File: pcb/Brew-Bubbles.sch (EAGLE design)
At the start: 7 parts, among them U1 GP1A57HR, U2 WEMOS-D1-MINI

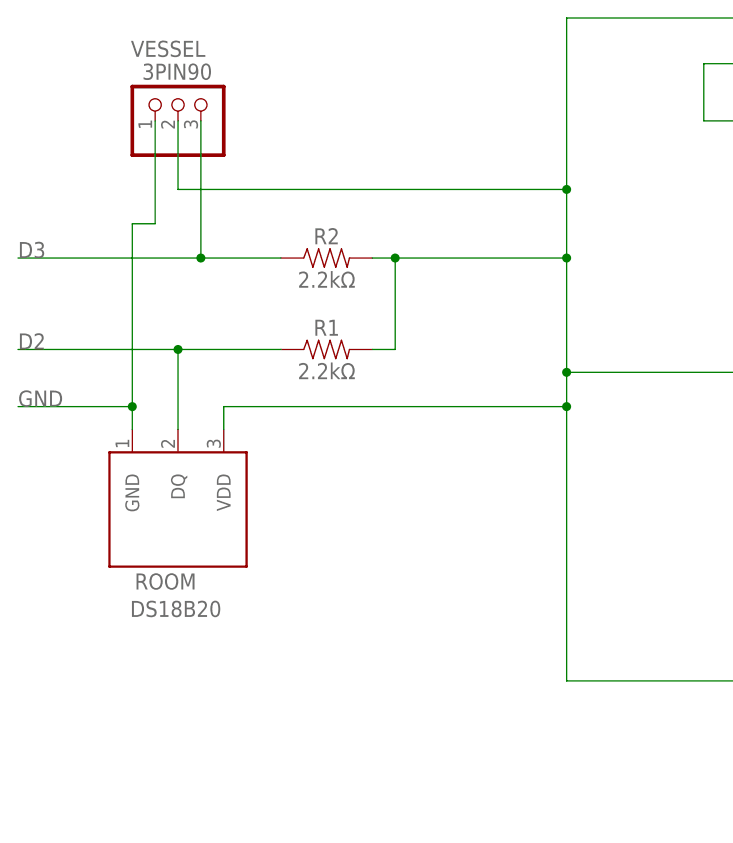
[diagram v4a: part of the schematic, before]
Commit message: Remove onboard sensor move to lead
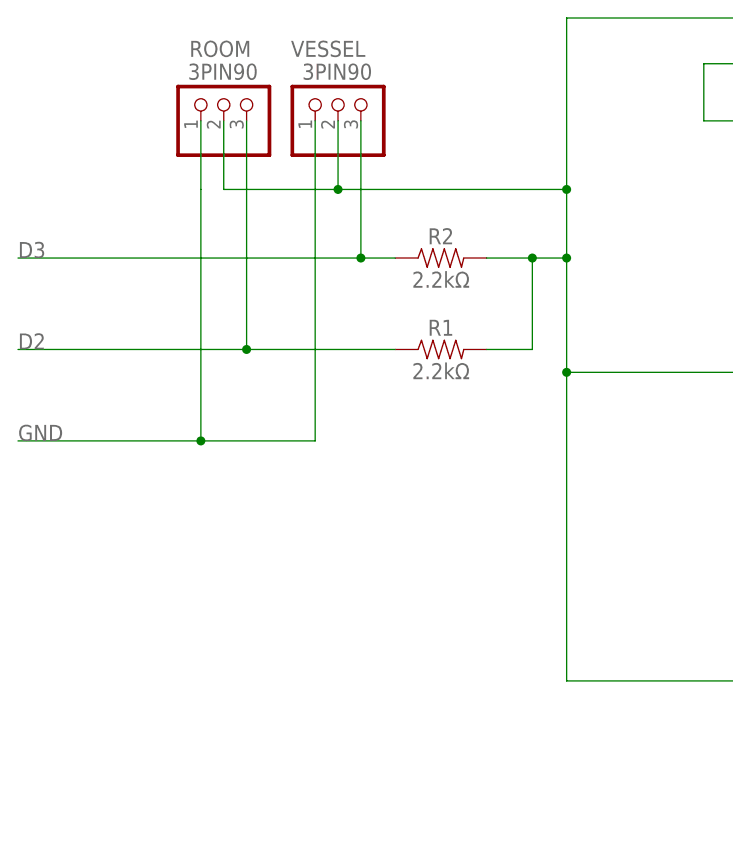
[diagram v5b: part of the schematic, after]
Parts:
- ROOM: value DS18B20 -> 3PIN90; device SparkFun-Sensors:DS18B20 -> pinhead:PINHD-1X3/90
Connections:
- net 3V3: now also ROOM.2; no longer ROOM.VDD
- net D2: now also ROOM.3; no longer ROOM.DQ
- net GND: now also ROOM.1; no longer ROOM.GND
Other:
- moved on the sheet: R1, R2, VESSEL
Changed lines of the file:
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@@
 </classes>
 <parts>
-<part name="ROOM" library="SparkFun-Sensors" deviceset="DS18B20" device=""/>
 <part name="U2" library="diy-modules" deviceset="WEMOS-D1-MINI-SHIELD" device="" value="WEMOS-D1-MINI"/>
 <part name="R1" library="SparkFun-Resistors" deviceset="330OHM" device="-HORIZ-1/10W-5%" value="2.2kΩ"/>
@@
 <part name="U1" library="SparkFun-Sensors" deviceset="GP1A57HR" device=""/>
 <part name="R3" library="SparkFun-Resistors" deviceset="330OHM" device="-HORIZ-1/10W-5%" value="150Ω"/>
+<part name="ROOM" library="pinhead" library_urn="urn:adsk.eagle:library:325" deviceset="PINHD-1X3" device="/90" package3d_urn="urn:adsk.eagle:package:22459/2" value="3PIN90"/>
 </parts>
 <sheets>
@@
 </plain>
 <instances>
-<instance part="ROOM" gate="G$1" x="-10.16" y="52.07" smashed="yes" rot="R270">
-<attribute name="NAME" x="-14.986" y="44.45" size="1.778" layer="95" font="vector"/>
-<attribute name="VALUE" x="-15.494" y="43.18" size="1.778" layer="96" font="vector" align="top-left"/>
-</instance>
 <instance part="U2" gate="G$1" x="77.47" y="41.91" smashed="yes">
 <attribute name="NAME" x="66.04" y="19.05" size="1.778" layer="95"/>
 <attribute name="VALUE" x="66.04" y="21.59" size="1.778" layer="96"/>
 </instance>
-<instance part="R1" gate="G$1" x="6.35" y="71.12" smashed="yes">
-<attribute name="NAME" x="6.35" y="72.644" size="1.778" layer="95" font="vector" align="bottom-center"/>
-<attribute name="VALUE" x="6.35" y="69.596" size="1.778" layer="96" font="vector" align="top-center"/>
+<instance part="R1" gate="G$1" x="19.05" y="71.12" smashed="yes">
+<attribute name="NAME" x="19.05" y="72.644" size="1.778" layer="95" font="vector" align="bottom-center"/>
+<attribute name="VALUE" x="19.05" y="69.596" size="1.778" layer="96" font="vector" align="top-center"/>
 </instance>
-<instance part="VESSEL" gate="A" x="-10.16" y="99.06" smashed="yes" rot="R90">
-<attribute name="VALUE" x="-6.35" y="102.87" size="1.778" layer="96" rot="R180"/>
-<attribute name="NAME" x="-7.112" y="105.41" size="1.778" layer="95" rot="R180"/>
+<instance part="VESSEL" gate="A" x="7.62" y="99.06" smashed="yes" rot="R90">
+<attribute name="VALUE" x="11.43" y="102.87" size="1.778" layer="96" rot="R180"/>
+<attribute name="NAME" x="10.668" y="105.41" size="1.778" layer="95" rot="R180"/>
 </instance>
-<instance part="R2" gate="G$1" x="6.35" y="81.28" smashed="yes">
-<attribute name="NAME" x="6.35" y="82.804" size="1.778" layer="95" font="vector" align="bottom-center"/>
-<attribute name="VALUE" x="6.35" y="79.756" size="1.778" layer="96" font="vector" align="top-center"/>
+<instance part="R2" gate="G$1" x="19.05" y="81.28" smashed="yes">
+<attribute name="NAME" x="19.05" y="82.804" size="1.778" layer="95" font="vector" align="bottom-center"/>
+<attribute name="VALUE" x="19.05" y="79.756" size="1.778" layer="96" font="vector" align="top-center"/>
 </instance>
 <instance part="U1" gate="G$1" x="74.93" y="83.82" smashed="yes">
@@
 <attribute name="NAME" x="62.23" y="98.044" size="1.778" layer="95" font="vector" align="bottom-center"/>
 <attribute name="VALUE" x="62.23" y="94.996" size="1.778" layer="96" font="vector" align="top-center"/>
+</instance>
+<instance part="ROOM" gate="A" x="-5.08" y="99.06" smashed="yes" rot="R90">
+<attribute name="VALUE" x="-1.27" y="102.87" size="1.778" layer="96" rot="R180"/>
+<attribute name="NAME" x="-2.032" y="105.41" size="1.778" layer="95" rot="R180"/>
 </instance>
 </instances>
@@
 <label x="52.07" y="34.29" size="1.778" layer="95"/>
 <wire x1="59.69" y1="34.29" x2="33.02" y2="34.29" width="0.1524" layer="91"/>
-<wire x1="33.02" y1="34.29" x2="33.02" y2="64.77" width="0.1524" layer="91"/>
-<wire x1="33.02" y1="64.77" x2="33.02" y2="68.58" width="0.1524" layer="91"/>
+<wire x1="33.02" y1="34.29" x2="33.02" y2="68.58" width="0.1524" layer="91"/>
 <wire x1="33.02" y1="68.58" x2="33.02" y2="81.28" width="0.1524" layer="91"/>
 <wire x1="33.02" y1="81.28" x2="33.02" y2="88.9" width="0.1524" layer="91"/>
@@
 <wire x1="80.01" y1="107.95" x2="80.01" y2="93.98" width="0.1524" layer="91"/>
 <pinref part="R2" gate="G$1" pin="2"/>
-<wire x1="11.43" y1="81.28" x2="13.97" y2="81.28" width="0.1524" layer="91"/>
-<wire x1="13.97" y1="81.28" x2="13.97" y2="71.12" width="0.1524" layer="91"/>
+<wire x1="24.13" y1="81.28" x2="29.21" y2="81.28" width="0.1524" layer="91"/>
+<wire x1="29.21" y1="81.28" x2="29.21" y2="71.12" width="0.1524" layer="91"/>
 <pinref part="R1" gate="G$1" pin="2"/>
-<wire x1="13.97" y1="71.12" x2="11.43" y2="71.12" width="0.1524" layer="91"/>
-<wire x1="13.97" y1="81.28" x2="33.02" y2="81.28" width="0.1524" layer="91"/>
-<junction x="13.97" y="81.28"/>
+<wire x1="29.21" y1="71.12" x2="24.13" y2="71.12" width="0.1524" layer="91"/>
+<wire x1="29.21" y1="81.28" x2="33.02" y2="81.28" width="0.1524" layer="91"/>
+<junction x="29.21" y="81.28"/>
 <junction x="33.02" y="81.28"/>
-<pinref part="ROOM" gate="G$1" pin="VDD"/>
-<wire x1="-5.08" y1="62.23" x2="-5.08" y2="64.77" width="0.1524" layer="91"/>
-<wire x1="-5.08" y1="64.77" x2="33.02" y2="64.77" width="0.1524" layer="91"/>
-<junction x="33.02" y="64.77"/>
 <pinref part="VESSEL" gate="A" pin="2"/>
-<wire x1="-10.16" y1="96.52" x2="-10.16" y2="88.9" width="0.1524" layer="91"/>
-<wire x1="-10.16" y1="88.9" x2="33.02" y2="88.9" width="0.1524" layer="91"/>
+<wire x1="7.62" y1="96.52" x2="7.62" y2="88.9" width="0.1524" layer="91"/>
+<wire x1="7.62" y1="88.9" x2="33.02" y2="88.9" width="0.1524" layer="91"/>
 <junction x="33.02" y="88.9"/>
+<pinref part="ROOM" gate="A" pin="2"/>
+<wire x1="-5.08" y1="96.52" x2="-5.08" y2="88.9" width="0.1524" layer="91"/>
+<wire x1="-5.08" y1="88.9" x2="7.62" y2="88.9" width="0.1524" layer="91"/>
+<junction x="7.62" y="88.9"/>
 </segment>
 </net>
@@
 <segment>
 <pinref part="R1" gate="G$1" pin="1"/>
-<wire x1="1.27" y1="71.12" x2="-10.16" y2="71.12" width="0.1524" layer="91"/>
-<pinref part="ROOM" gate="G$1" pin="DQ"/>
-<wire x1="-10.16" y1="71.12" x2="-10.16" y2="62.23" width="0.1524" layer="91"/>
-<wire x1="-10.16" y1="71.12" x2="-27.94" y2="71.12" width="0.1524" layer="91"/>
-<junction x="-10.16" y="71.12"/>
+<wire x1="13.97" y1="71.12" x2="-2.54" y2="71.12" width="0.1524" layer="91"/>
+<wire x1="-2.54" y1="71.12" x2="-27.94" y2="71.12" width="0.1524" layer="91"/>
 <label x="-27.94" y="71.12" size="1.778" layer="95"/>
+<pinref part="ROOM" gate="A" pin="3"/>
+<wire x1="-2.54" y1="96.52" x2="-2.54" y2="71.12" width="0.1524" layer="91"/>
+<junction x="-2.54" y="71.12"/>
 </segment>
 </net>
@@
 <segment>
 <pinref part="R2" gate="G$1" pin="1"/>
-<wire x1="1.27" y1="81.28" x2="-7.62" y2="81.28" width="0.1524" layer="91"/>
+<wire x1="13.97" y1="81.28" x2="10.16" y2="81.28" width="0.1524" layer="91"/>
 <label x="-27.94" y="81.28" size="1.778" layer="95"/>
 <pinref part="VESSEL" gate="A" pin="3"/>
-<wire x1="-7.62" y1="81.28" x2="-27.94" y2="81.28" width="0.1524" layer="91"/>
-<wire x1="-7.62" y1="96.52" x2="-7.62" y2="81.28" width="0.1524" layer="91"/>
-<junction x="-7.62" y="81.28"/>
+<wire x1="10.16" y1="81.28" x2="-27.94" y2="81.28" width="0.1524" layer="91"/>
+<wire x1="10.16" y1="96.52" x2="10.16" y2="81.28" width="0.1524" layer="91"/>
+<junction x="10.16" y="81.28"/>
 </segment>
 </net>
@@
 </segment>
 <segment>
+<pinref part="ROOM" gate="A" pin="1"/>
+<wire x1="-7.62" y1="96.52" x2="-7.62" y2="88.9" width="0.1524" layer="91"/>
+<label x="-27.94" y="60.96" size="1.778" layer="95"/>
+<wire x1="-27.94" y1="60.96" x2="-7.62" y2="60.96" width="0.1524" layer="91"/>
+<wire x1="-7.62" y1="60.96" x2="5.08" y2="60.96" width="0.1524" layer="91"/>
+<wire x1="5.08" y1="60.96" x2="5.08" y2="96.52" width="0.1524" layer="91"/>
 <pinref part="VESSEL" gate="A" pin="1"/>
-<wire x1="-12.7" y1="96.52" x2="-12.7" y2="85.09" width="0.1524" layer="91"/>
-<wire x1="-12.7" y1="85.09" x2="-15.24" y2="85.09" width="0.1524" layer="91"/>
-<pinref part="ROOM" gate="G$1" pin="GND"/>
-<wire x1="-15.24" y1="85.09" x2="-15.24" y2="64.77" width="0.1524" layer="91"/>
-<wire x1="-15.24" y1="64.77" x2="-15.24" y2="62.23" width="0.1524" layer="91"/>
-<wire x1="-15.24" y1="64.77" x2="-27.94" y2="64.77" width="0.1524" layer="91"/>
-<junction x="-15.24" y="64.77"/>
-<label x="-27.94" y="64.77" size="1.778" layer="95"/>
+<wire x1="-7.62" y1="88.9" x2="-7.62" y2="60.96" width="0.1524" layer="91"/>
+<junction x="-7.62" y="60.96"/>
 </segment>
 </net>

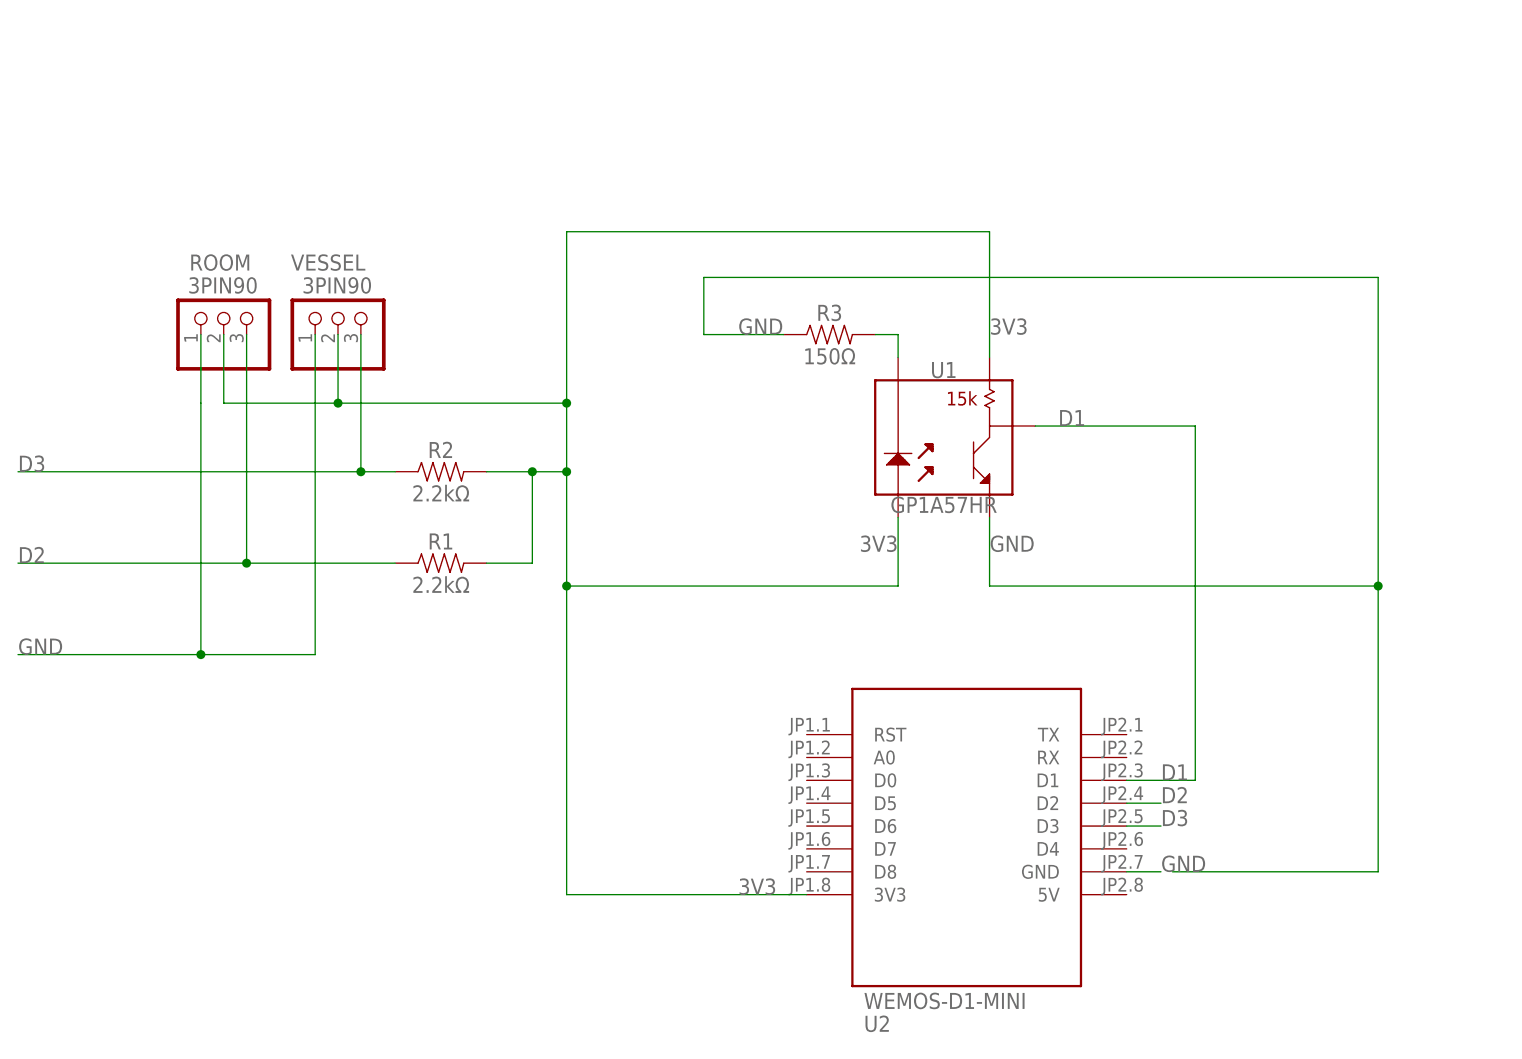
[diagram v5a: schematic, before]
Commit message: Change DS18B20 for ROOM to waterproof lead
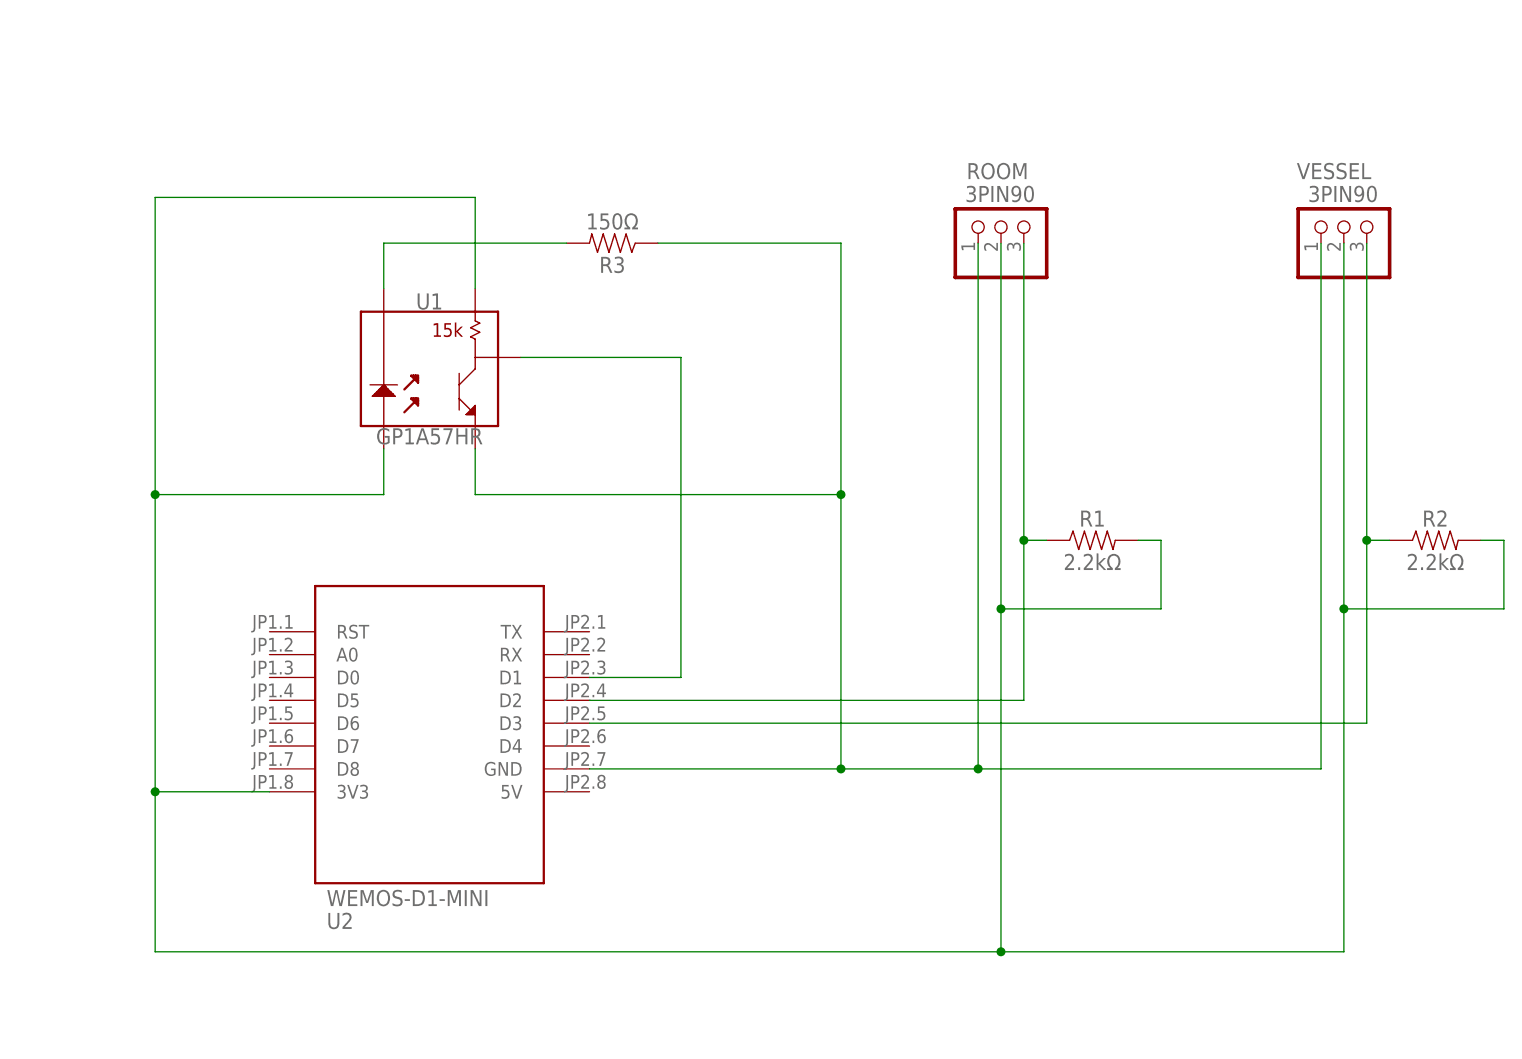
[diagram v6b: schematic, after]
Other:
- moved on the sheet: R1, R2, R3, ROOM, U1, U2, VESSEL

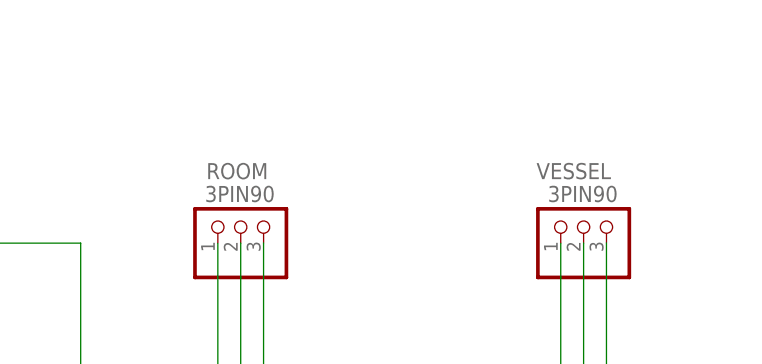
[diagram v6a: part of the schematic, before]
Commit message: Update PCB to show sensor pins on back
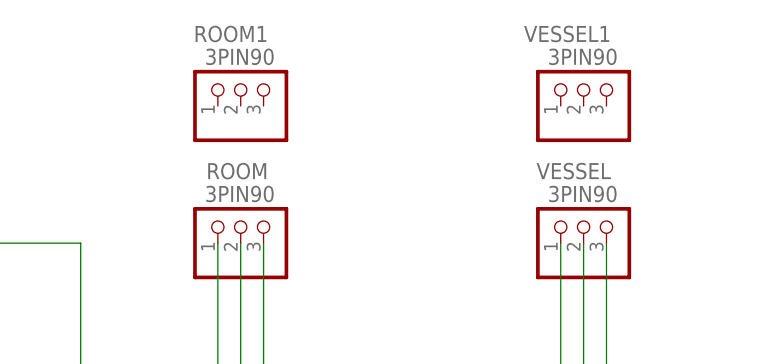
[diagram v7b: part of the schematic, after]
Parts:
- added ROOM1, VESSEL1: 3PIN90, pinhead:PINHD-1X3/90
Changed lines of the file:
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@@
 <?xml version="1.0" encoding="utf-8"?>
 <!DOCTYPE eagle SYSTEM "eagle.dtd">
-<eagle version="9.4.2">
+<eagle version="9.5.0">
 <drawing>
 <settings>
@@
 <part name="ROOM" library="pinhead" library_urn="urn:adsk.eagle:library:325" deviceset="PINHD-1X3" device="/90" package3d_urn="urn:adsk.eagle:package:22459/2" value="3PIN90"/>
 <part name="FRAME1" library="frames" deviceset="LETTER_L" device=""/>
+<part name="ROOM1" library="pinhead" library_urn="urn:adsk.eagle:library:325" deviceset="PINHD-1X3" device="/90" package3d_urn="urn:adsk.eagle:package:22459/2" value="3PIN90"/>
+<part name="VESSEL1" library="pinhead" library_urn="urn:adsk.eagle:library:325" deviceset="PINHD-1X3" device="/90" package3d_urn="urn:adsk.eagle:package:22459/2" value="3PIN90"/>
 </parts>
 <sheets>
@@
 <attribute name="DRAWING_NAME" x="96.52" y="-6.35" size="2.54" layer="94" font="vector"/>
 </instance>
+<instance part="ROOM1" gate="A" x="81.28" y="124.46" smashed="yes" rot="R90">
+<attribute name="VALUE" x="85.09" y="128.27" size="1.778" layer="96" rot="R180"/>
+<attribute name="NAME" x="84.328" y="130.81" size="1.778" layer="95" rot="R180"/>
+</instance>
+<instance part="VESSEL1" gate="A" x="119.38" y="124.46" smashed="yes" rot="R90">
+<attribute name="VALUE" x="123.19" y="128.27" size="1.778" layer="96" rot="R180"/>
+<attribute name="NAME" x="122.428" y="130.81" size="1.778" layer="95" rot="R180"/>
+</instance>
 </instances>
